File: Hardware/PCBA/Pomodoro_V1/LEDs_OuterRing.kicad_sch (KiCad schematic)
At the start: 10 parts

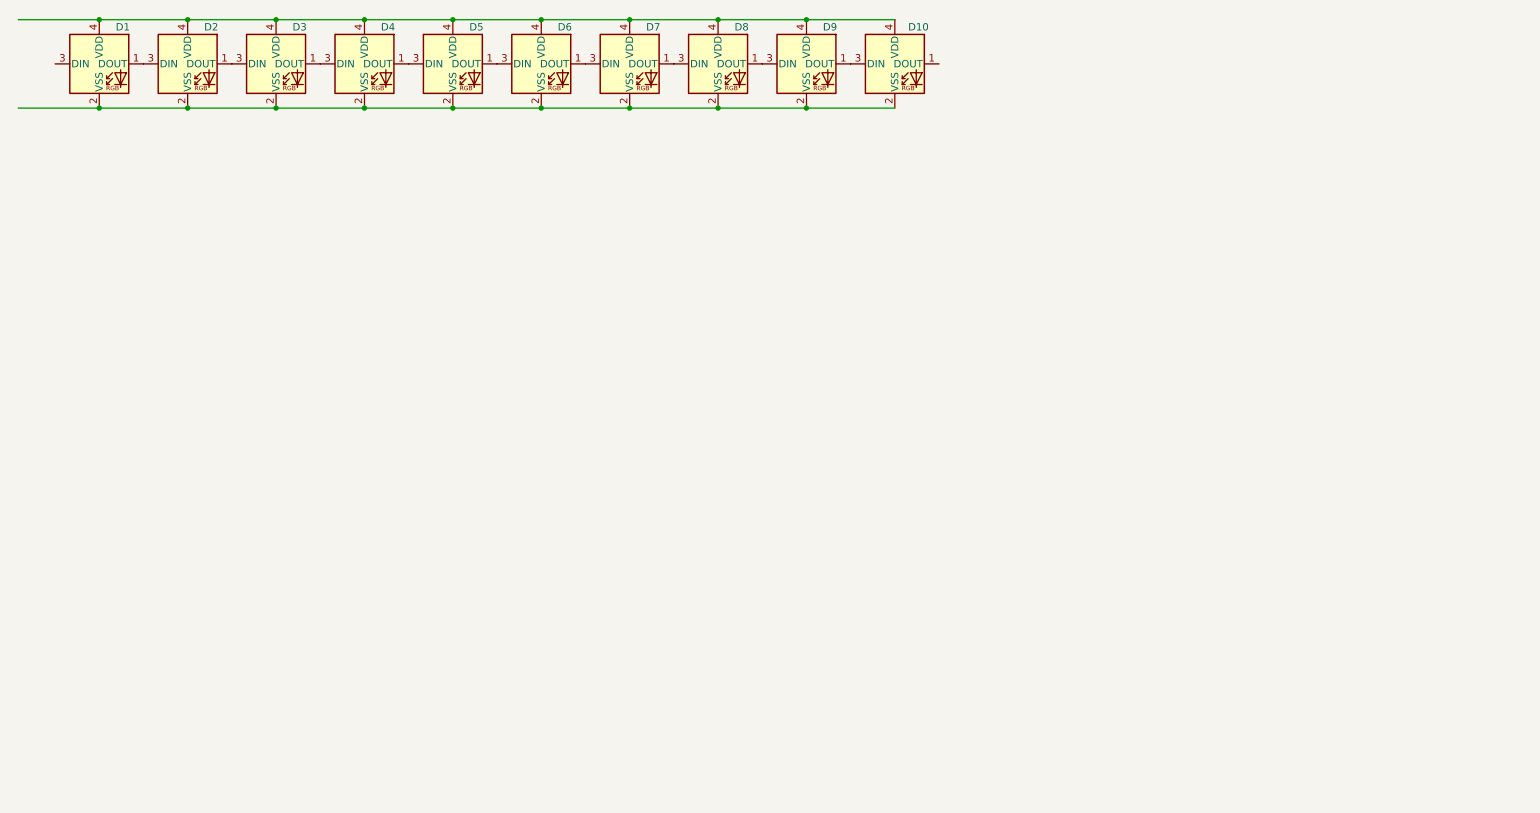
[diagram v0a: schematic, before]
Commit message: Updated CubeMx File, Created Schematic for µC, layouted the LEDs on the PCB
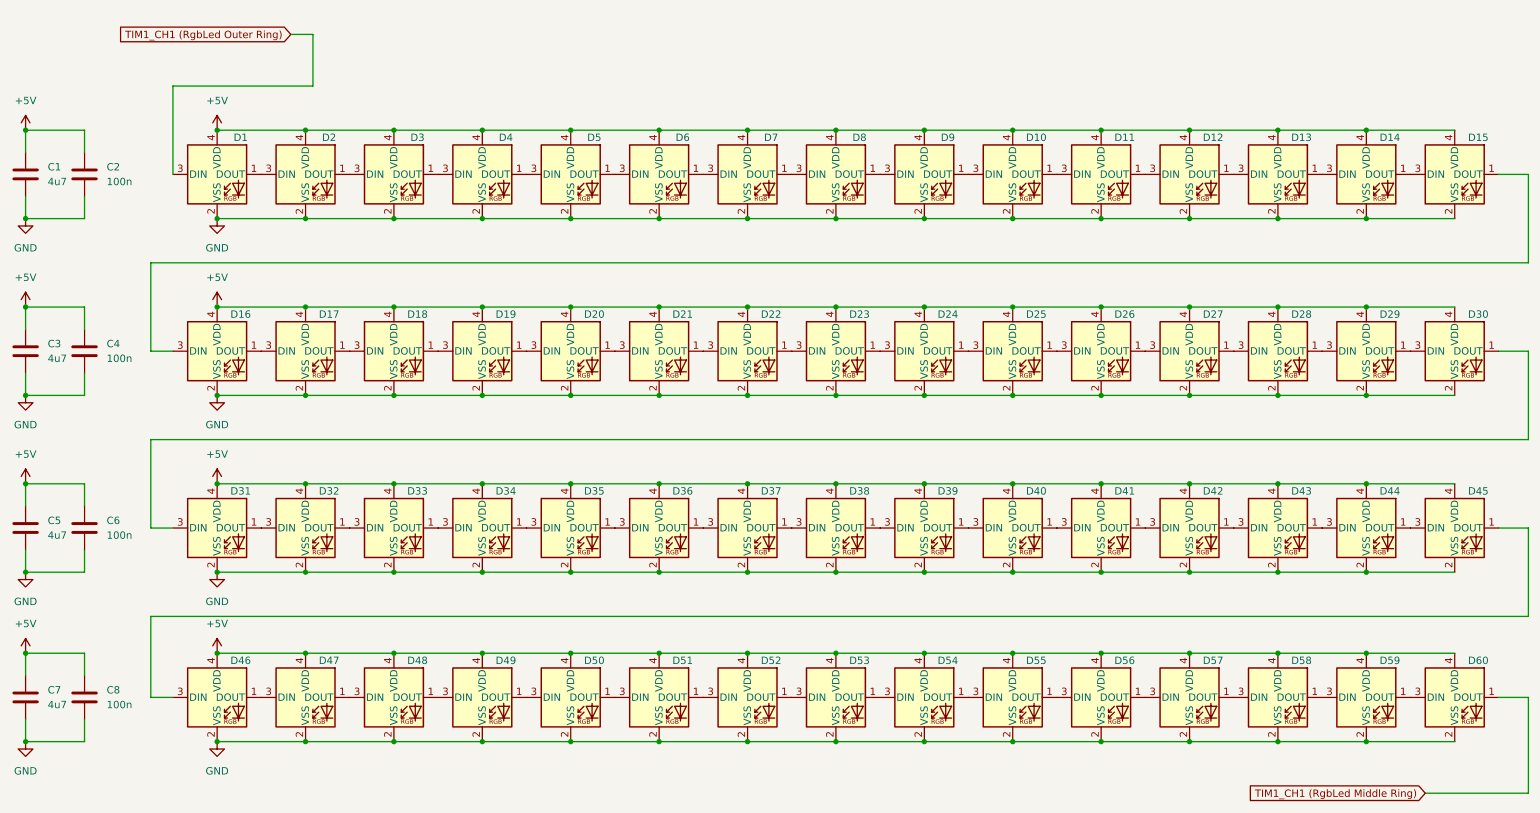
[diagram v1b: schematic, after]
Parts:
- added C1, C3, C5, C7: 4u7, symbol Device:C
- added C2, C4, C6, C8: 100n, symbol Device:C
- added D11, D12, D13, D14, D15, D16, D17, D18, D19, D20, D21, D22, D23, D24, D25, D26, D27, D28, D29, D30, D31, D32, D33, D34, D35, D36, D37, D38, D39, D40, D41, D42, D43, D44, D45, D46, D47, D48, D49, D50, D51, D52, D53, D54, D55, D56, D57, D58, D59, D60: WS2812B-2020, LED_SMD:LED_WS2812B-2020_PLCC4_2.0x2.0mm, symbol LED:WS2812B-2020
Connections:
- net GND: now reaches D1.2 (VSS), D10.2 (VSS), D2.2 (VSS), D3.2 (VSS), D4.2 (VSS), D5.2 (VSS), D6.2 (VSS), D7.2 (VSS), D8.2 (VSS), D9.2 (VSS)
- net GND: now also C1.2, C2.2, C3.2, C4.2, C5.2, C6.2, C7.2, C8.2, D11.2 (VSS), D12.2 (VSS), D13.2 (VSS), D14.2 (VSS), D15.2 (VSS), D16.2 (VSS), D17.2 (VSS), D18.2 (VSS), D19.2 (VSS), D20.2 (VSS), D21.2 (VSS), D22.2 (VSS), D23.2 (VSS), D24.2 (VSS), D25.2 (VSS), D26.2 (VSS), D27.2 (VSS), D28.2 (VSS), D29.2 (VSS), D30.2 (VSS), D31.2 (VSS), D32.2 (VSS), D33.2 (VSS), D34.2 (VSS), D35.2 (VSS), D36.2 (VSS), D37.2 (VSS), D38.2 (VSS), D39.2 (VSS), D40.2 (VSS), D41.2 (VSS), D42.2 (VSS), D43.2 (VSS), D44.2 (VSS), D45.2 (VSS), D46.2 (VSS), D47.2 (VSS), D48.2 (VSS), D49.2 (VSS), D50.2 (VSS), D51.2 (VSS), D52.2 (VSS), D53.2 (VSS), D54.2 (VSS), D55.2 (VSS), D56.2 (VSS), D57.2 (VSS), D58.2 (VSS), D59.2 (VSS), D60.2 (VSS)
- net TIM1_CH1 (RgbLed Outer Ring): now reaches D1.3 (DIN)
- net +5V: now reaches D1.4 (VDD), D10.4 (VDD), D2.4 (VDD), D3.4 (VDD), D4.4 (VDD), D5.4 (VDD), D6.4 (VDD), D7.4 (VDD), D8.4 (VDD), D9.4 (VDD)
- net +5V: now also C1.1, C2.1, C3.1, C4.1, C5.1, C6.1, C7.1, C8.1, D11.4 (VDD), D12.4 (VDD), D13.4 (VDD), D14.4 (VDD), D15.4 (VDD), D16.4 (VDD), D17.4 (VDD), D18.4 (VDD), D19.4 (VDD), D20.4 (VDD), D21.4 (VDD), D22.4 (VDD), D23.4 (VDD), D24.4 (VDD), D25.4 (VDD), D26.4 (VDD), D27.4 (VDD), D28.4 (VDD), D29.4 (VDD), D30.4 (VDD), D31.4 (VDD), D32.4 (VDD), D33.4 (VDD), D34.4 (VDD), D35.4 (VDD), D36.4 (VDD), D37.4 (VDD), D38.4 (VDD), D39.4 (VDD), D40.4 (VDD), D41.4 (VDD), D42.4 (VDD), D43.4 (VDD), D44.4 (VDD), D45.4 (VDD), D46.4 (VDD), D47.4 (VDD), D48.4 (VDD), D49.4 (VDD), D50.4 (VDD), D51.4 (VDD), D52.4 (VDD), D53.4 (VDD), D54.4 (VDD), D55.4 (VDD), D56.4 (VDD), D57.4 (VDD), D58.4 (VDD), D59.4 (VDD), D60.4 (VDD)
- net at D10.1 (DOUT): now also D11.3 (DIN)
- new net: D20.1 (DOUT), D21.3 (DIN)
- new net: D19.1 (DOUT), D20.3 (DIN)
- new net: D59.1 (DOUT), D60.3 (DIN)
- new net: D12.1 (DOUT), D13.3 (DIN)
- new net: D11.1 (DOUT), D12.3 (DIN)
- new net: D57.1 (DOUT), D58.3 (DIN)
- new net: D56.1 (DOUT), D57.3 (DIN)
- new net: D45.1 (DOUT), D46.3 (DIN)
- new net: D44.1 (DOUT), D45.3 (DIN)
- new net: D32.1 (DOUT), D33.3 (DIN)
- new net: D31.1 (DOUT), D32.3 (DIN)
- new net: D17.1 (DOUT), D18.3 (DIN)
- new net: D16.1 (DOUT), D17.3 (DIN)
- new net: D30.1 (DOUT), D31.3 (DIN)
- new net: D29.1 (DOUT), D30.3 (DIN)
- new net: D38.1 (DOUT), D39.3 (DIN)
- new net: D37.1 (DOUT), D38.3 (DIN)
- new net: D15.1 (DOUT), D16.3 (DIN)
- new net: D24.1 (DOUT), D25.3 (DIN)
- new net: D23.1 (DOUT), D24.3 (DIN)
- new net: D35.1 (DOUT), D36.3 (DIN)
- new net: D34.1 (DOUT), D35.3 (DIN)
- new net: D13.1 (DOUT), D14.3 (DIN)
- new net: D54.1 (DOUT), D55.3 (DIN)
- new net: D53.1 (DOUT), D54.3 (DIN)
- new net: D14.1 (DOUT), D15.3 (DIN)
- new net: D47.1 (DOUT), D48.3 (DIN)
- new net: D46.1 (DOUT), D47.3 (DIN)
- new net: D33.1 (DOUT), D34.3 (DIN)
- new net: D50.1 (DOUT), D51.3 (DIN)
- new net: D49.1 (DOUT), D50.3 (DIN)
- new net: D58.1 (DOUT), D59.3 (DIN)
- new net: D18.1 (DOUT), D19.3 (DIN)
- new net: D22.1 (DOUT), D23.3 (DIN)
- new net: D52.1 (DOUT), D53.3 (DIN)
- new net: D51.1 (DOUT), D52.3 (DIN)
- new net: D43.1 (DOUT), D44.3 (DIN)
- new net: D42.1 (DOUT), D43.3 (DIN)
- new net: D26.1 (DOUT), D27.3 (DIN)
- new net: D25.1 (DOUT), D26.3 (DIN)
- new net: D28.1 (DOUT), D29.3 (DIN)
- new net: D55.1 (DOUT), D56.3 (DIN)
- new net: D36.1 (DOUT), D37.3 (DIN)
- new net: D21.1 (DOUT), D22.3 (DIN)
- new net: D48.1 (DOUT), D49.3 (DIN)
- new net: D40.1 (DOUT), D41.3 (DIN)
- new net: D39.1 (DOUT), D40.3 (DIN)
- new net: D27.1 (DOUT), D28.3 (DIN)
- new net: D41.1 (DOUT), D42.3 (DIN)
- new net TIM1_CH1 (RgbLed Middle Ring): D60.1 (DOUT)
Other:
- moved on the sheet: D1, D10, D2, D3, D4, D5, D6, D7, D8, D9

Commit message: Finalized the schematic, First Draft of the finished Layout
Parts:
- removed C1, C3, C5, C7: 4u7, symbol Device:C
- removed C2, C4, C6, C8: 100n, symbol Device:C
- added R8: 100, Resistor_SMD:R_0805_2012Metric, symbol Device:R
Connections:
- net TIM1_CH1 (RgbLed Outer Ring): now also R8.1; no longer D1.3 (DIN)
- new net: D1.3 (DIN), R8.2

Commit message: Version that was ordered online
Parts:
- D1, D10, D11, D12, D13, D14, D15, D16, D17, D18, D19, D2, D20, D21, D22, D23, D24, D25, D26, D27, D28, D29, D3, D30, D31, D32, D33, D34, D35, D36, D37, D38, D39, D4, D40, D41, D42, D43, D44, D45, D46, D47, D48, D49, D5, D50, D51, D52, D53, D54, D55, D56, D57, D58, D59, D6, D60, D7, D8, D9: MPN (none) -> WS2812B-2020
- R8: MPN (none) -> RC0805FR-07100RL
